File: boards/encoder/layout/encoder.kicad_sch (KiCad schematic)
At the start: 3 parts, among them J1 EncoderTab, U1 AS5047U-HTSM

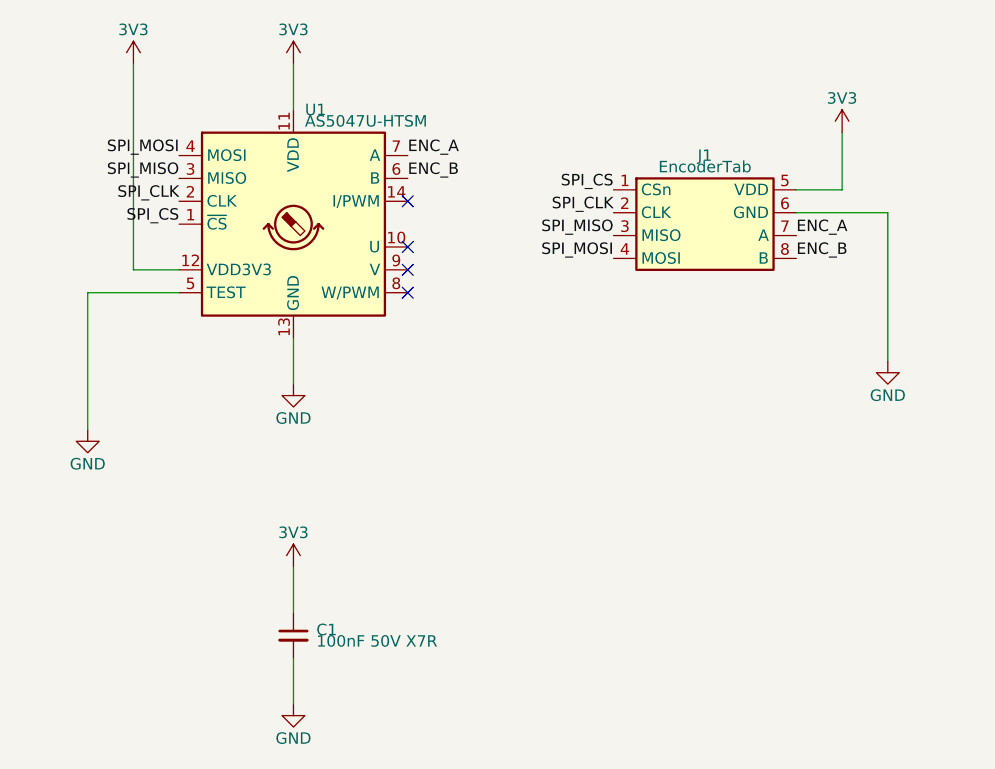
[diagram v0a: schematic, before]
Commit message: 🚚 Replicate the previous encoder board
The circuit, designators (IC1, C1, J1) and net names of the Altium
MicrasEncoder design, with C1 as the equivalent JLCPCB basic part
(Yageo CC0603KRX7R9BB104 for the Fenghua 0603B104K500NT). The layout
comes from the PcbDoc through boards/encoder/previous/transfer_layout.py:
tracks, vias, pours, teardrops (as plain zones), outline, silkscreen and
logo copied, IC1 and J1 at their previous positions, C1 fitted on the
previous pads.

spec/encoder.toml now checks the outline (layout geometry) instead of
generating it: tab, reliefs, shoulder, tapers (fitted Bezier, 0.021 mm),
corners and extents; thickness 0.79 mm from the PcbDoc stack; the mech
JSON exports the layout outline. `make previous` compares every board
with a previous/board.json.
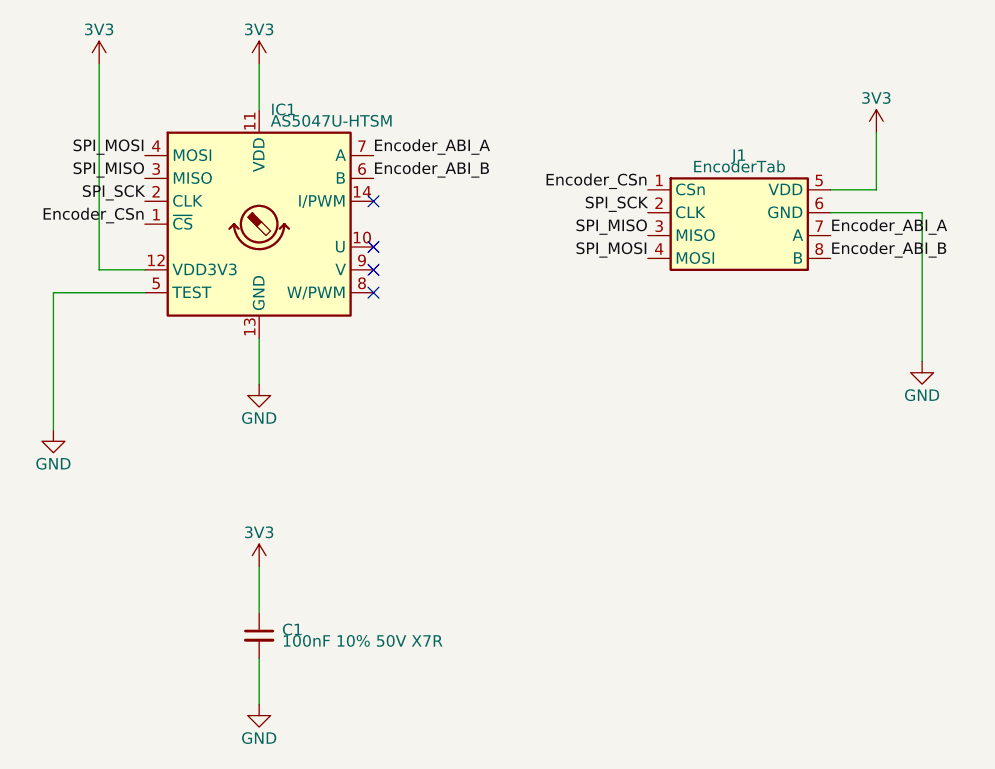
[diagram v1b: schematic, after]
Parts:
- removed U1: AS5047U-HTSM, Team-Micras_MicrasPCB_components_ams_AS5047U:TSSOP-14_4.4x5mm_P0.65mm, symbol AS5047U
- added IC1: AS5047U-HTSM, Team-Micras_MicrasPCB_components_ams_AS5047U:SOP65P640X120-14N, symbol AS5047U
- C1: value 100nF 50V X7R -> 100nF 10% 50V X7R; Path SENSOR.C_VDD.C -> C1.C
- J1: footprint Team-Micras_MicrasPCB_components_micras_EncoderTab:EncoderTab_2x4_P0.95mm_Edge -> Team-Micras_MicrasPCB_components_micras_EncoderTab:ENCODER_CONN; Path TAB.TAB -> J1.TAB
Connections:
- net 3V3: now also IC1.11 (VDD), IC1.12 (VDD3V3)
- net GND: now also IC1.13 (GND), IC1.5 (TEST)
- net SPI_MISO: now also IC1.3 (MISO)
- net SPI_MOSI: now also IC1.4 (MOSI)
- net ENC_A renamed Encoder_ABI_A
- net Encoder_ABI_A: now also IC1.7 (A)
- net ENC_B renamed Encoder_ABI_B
- net Encoder_ABI_B: now also IC1.6 (B)
- net SPI_CLK renamed SPI_SCK
- net SPI_SCK: now also IC1.2 (CLK)
- net SPI_CS renamed Encoder_CSn
- net Encoder_CSn: now also IC1.1 (~{CS})

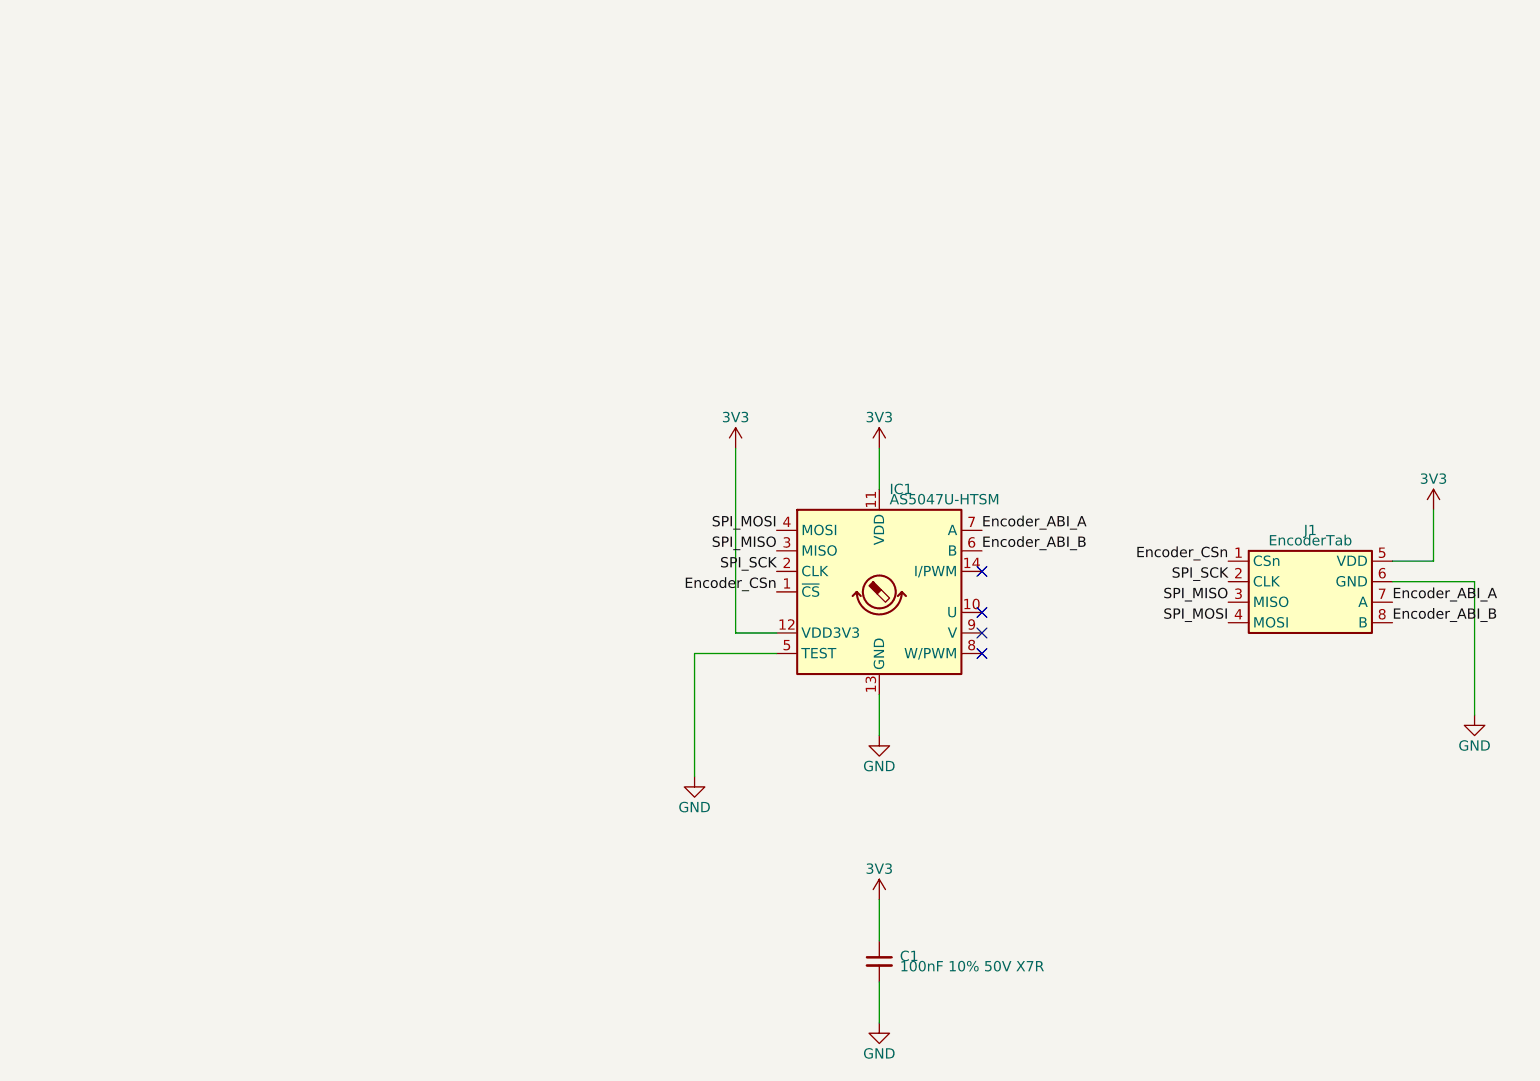
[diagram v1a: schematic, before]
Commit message: ✨ Place the schematics from per-sheet placement files
micras-pcb sch redraws each sheet pcb apply writes from
boards/<board>/schematic/<sheet>.toml: parts, wires, labels, power
symbols, titled frames, paper and title block, the root's sheet
symbols, and a ports column for the module sheets' extra labels. It
fails unless KiCad's netlist of the placed schematic equals pcb's.
make gen runs it after pcb apply; make check's sch gate fails on a part
without a placement, and tests/test_placement.py on any overlap.

The encoder and Bluetooth sheets are placed; the main board's DRIVERS
sheet is drafted.
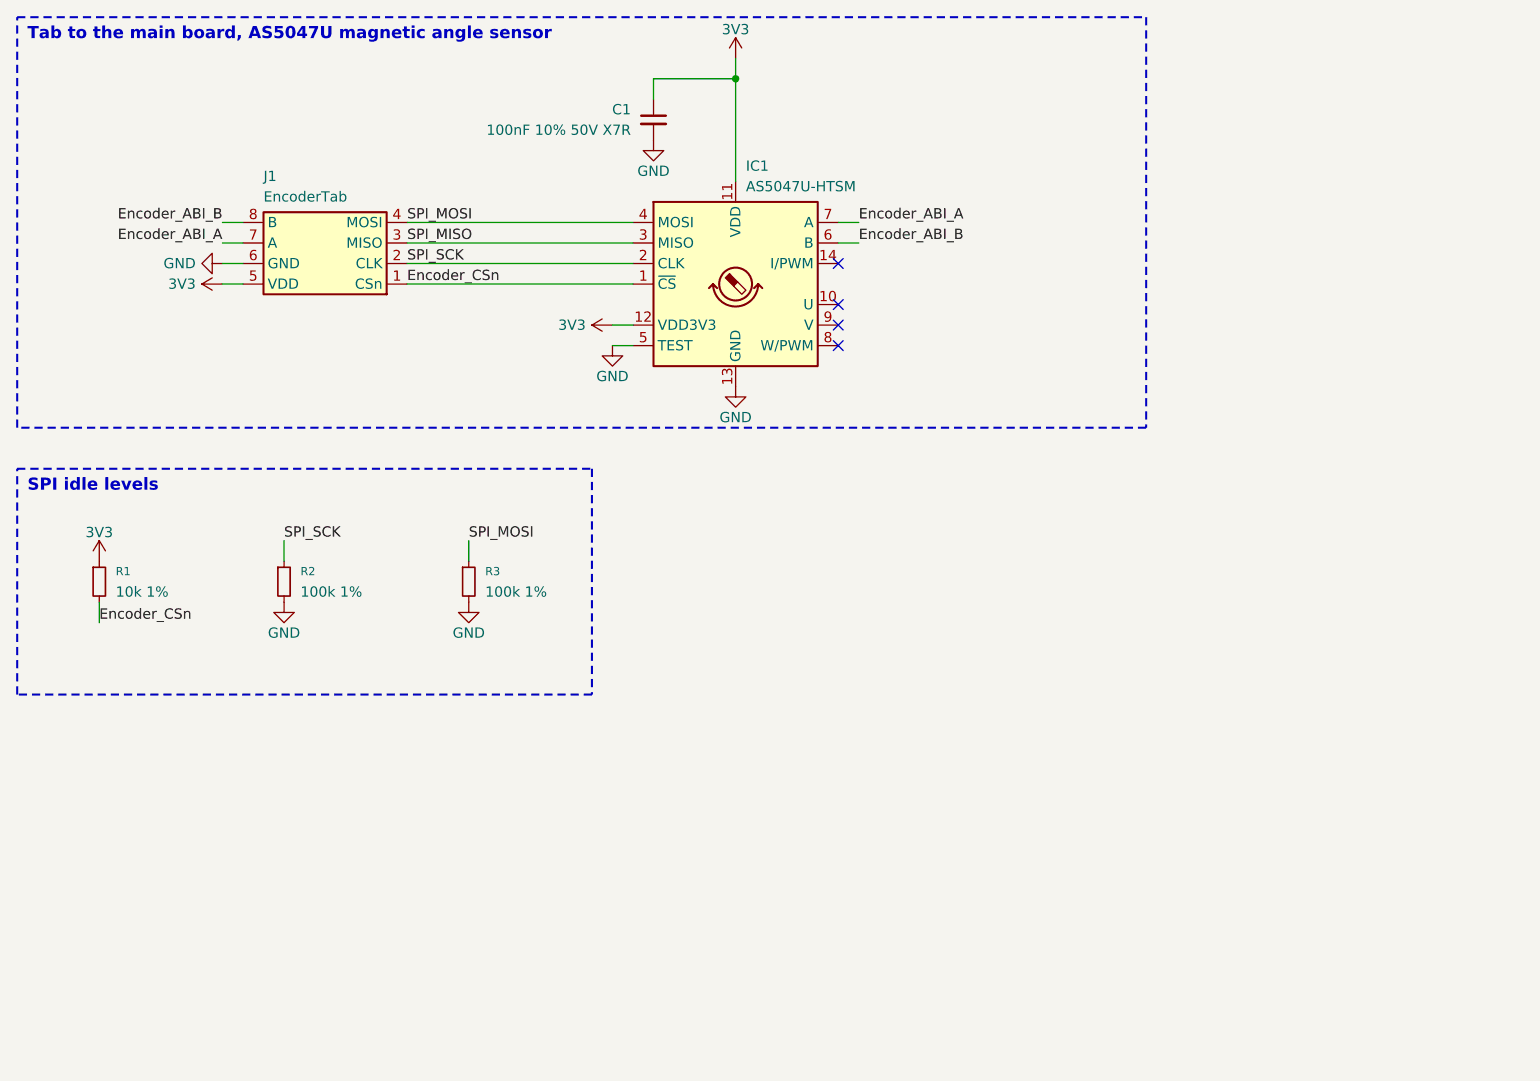
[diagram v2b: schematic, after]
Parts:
- added R1: 10k 1%, stdlib_kicad-footprints_Resistor_SMD:R_0402_1005Metric, symbol R_Small
- added R2, R3: 100k 1%, stdlib_kicad-footprints_Resistor_SMD:R_0402_1005Metric, symbol R_Small
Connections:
- net 3V3: now also R1.1
- net Encoder_CSn: now also R1.2
- net GND: now also R2.2, R3.2
- net SPI_MOSI: now also R3.1
- net SPI_SCK: now also R2.1
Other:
- note added: "SPI idle levels"
- note added: "Tab to the main board, AS5047U magnetic angle sensor"
- title: (none) -> Wheel encoder
- moved on the sheet: C1, IC1, J1
